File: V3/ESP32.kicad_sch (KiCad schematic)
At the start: 20 parts, among them J6 Conn_01x02_Female, Q6 MMBT2222, SW2 RST, SW3 BOOT, U9 ESP32-WROOM-32

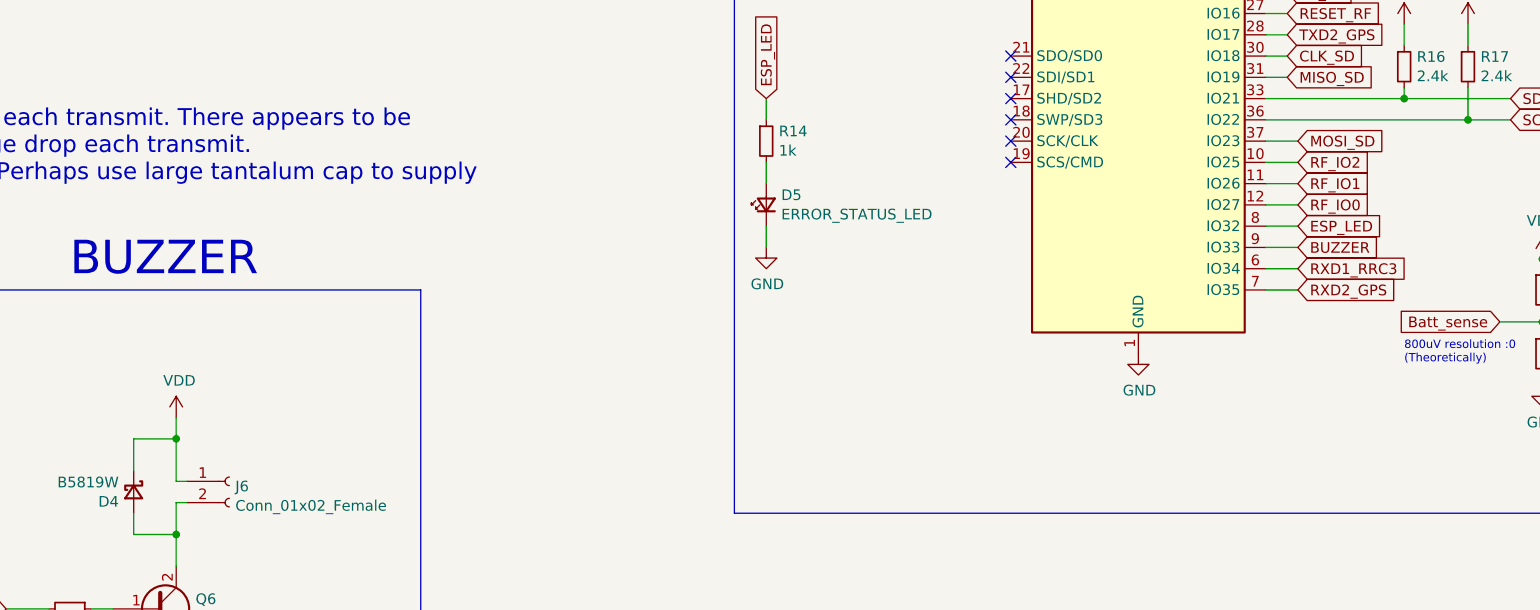
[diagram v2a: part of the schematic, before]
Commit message: Added mpu6050 back
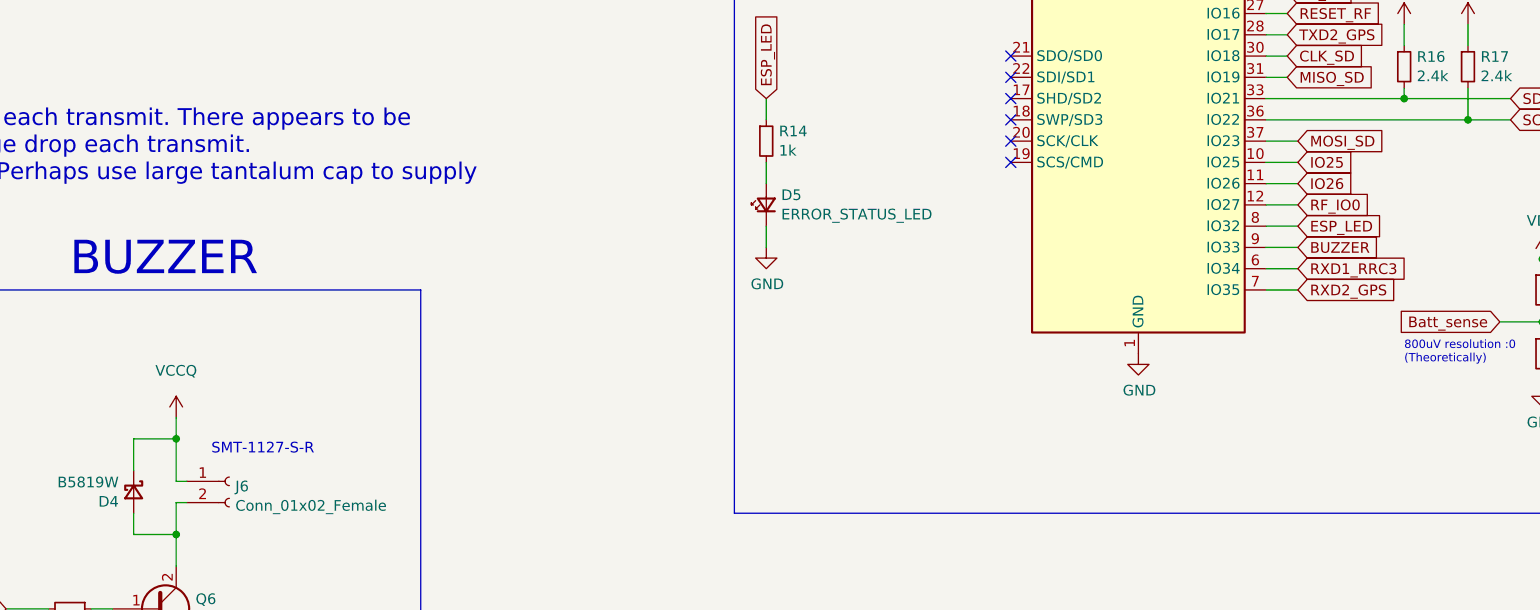
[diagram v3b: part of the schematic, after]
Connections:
- net VDD: no longer D4.1 (K), J6.1 (Pin_1)
- net RF_IO1 renamed IO26
- net RF_IO2 renamed IO25
- new net VCCQ: D4.1 (K), J6.1 (Pin_1)
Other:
- note added: "SMT-1127-S-R"
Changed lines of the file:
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@@
     (stroke (width 0) (type default) (color 0 0 0 0))
+  )
+  (text "SMT-1127-S-R" (at 83.566 138.557 0)
+    (effects (font (size 1.27 1.27)) (justify left bottom))
   )
   (text "Power LED flickers each transmit. There appears to be \na significant voltage drop each transmit.\nVerify with scope. Perhaps use large tantalum cap to supply \ntransmit current. "
@@
     )
   )
-  (global_label "RF_IO2" (shape input) (at 213.36 103.505 0) (fields_autoplaced)
-    (effects (font (size 1.27 1.27)) (justify left))
-    (property "Intersheet References" "${INTERSHEET_REFS}" (id 0) (at 124.46 -6.985 0)
-      (effects (font (size 1.27 1.27)) hide)
+  (global_label "IO25" (shape input) (at 213.36 103.505 0) (fields_autoplaced)
+    (effects (font (size 1.27 1.27)) (justify left))
+    (property "Intersheet References" "${INTERSHEET_REFS}" (id 0) (at 220.0385 103.4256 0)
+      (effects (font (size 1.27 1.27)) (justify left) hide)
     )
   )
@@
     )
   )
-  (global_label "RF_IO1" (shape input) (at 213.36 106.045 0) (fields_autoplaced)
-    (effects (font (size 1.27 1.27)) (justify left))
-    (property "Intersheet References" "${INTERSHEET_REFS}" (id 0) (at 124.46 -6.985 0)
-      (effects (font (size 1.27 1.27)) hide)
+  (global_label "IO26" (shape input) (at 213.36 106.045 0) (fields_autoplaced)
+    (effects (font (size 1.27 1.27)) (justify left))
+    (property "Intersheet References" "${INTERSHEET_REFS}" (id 0) (at 220.0385 105.9656 0)
+      (effects (font (size 1.27 1.27)) (justify left) hide)
     )
   )
@@
     (pin "9")
   )
+  (symbol (lib_id "power:VCCQ") (at 79.375 133.985 0) (unit 1)
+    (in_bom yes) (on_board yes) (fields_autoplaced)
+    (property "Reference" "#PWR?" (id 0) (at 79.375 137.795 0)
+      (effects (font (size 1.27 1.27)) hide)
+    )
+    (property "Value" "VCCQ" (id 1) (at 79.375 128.397 0))
+    (property "Footprint" "" (id 2) (at 79.375 133.985 0)
+      (effects (font (size 1.27 1.27)) hide)
+    )
+    (property "Datasheet" "" (id 3) (at 79.375 133.985 0)
+      (effects (font (size 1.27 1.27)) hide)
+    )
+    (pin "1")
+  )
   (symbol (lib_id "Connector:Conn_01x02_Female") (at 85.725 141.605 0) (unit 1)
     (in_bom yes) (on_board yes)
@@
       (effects (font (size 1.27 1.27)) hide)
     )
-    (pin "1")
-  )
-  (symbol (lib_id "power:VDD") (at 79.375 133.985 0) (unit 1)
-    (in_bom yes) (on_board yes)
-    (property "Reference" "#PWR0144" (id 0) (at 79.375 137.795 0)
-      (effects (font (size 1.27 1.27)) hide)
-    )
-    (property "Value" "VDD" (id 1) (at 79.756 129.5908 0))
-    (property "Footprint" "" (id 2) (at 79.375 133.985 0)
-      (effects (font (size 1.27 1.27)) hide)
-    )
-    (property "Datasheet" "" (id 3) (at 79.375 133.985 0)
-      (effects (font (size 1.27 1.27)) hide)
-    )

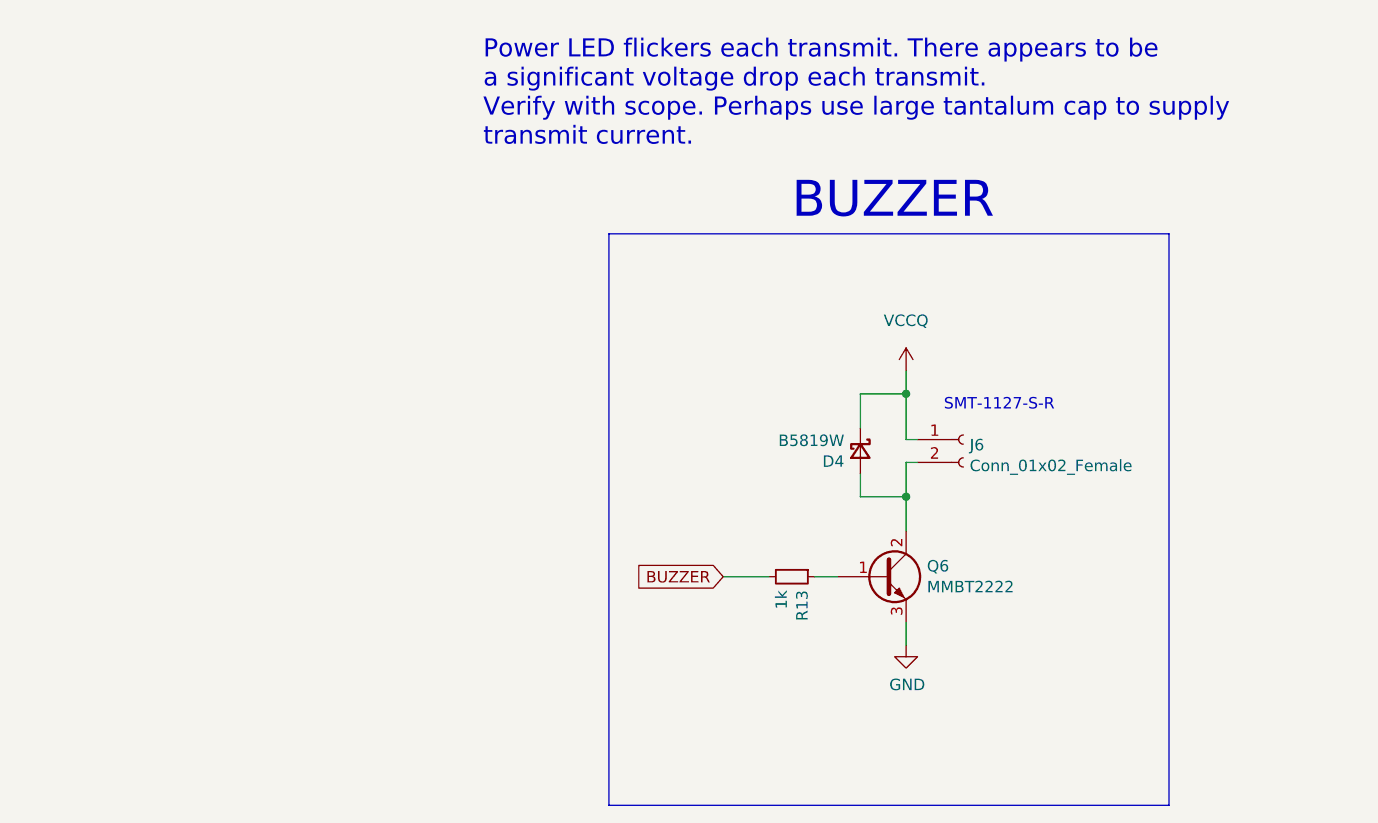
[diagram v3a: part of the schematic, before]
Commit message: buzzer added
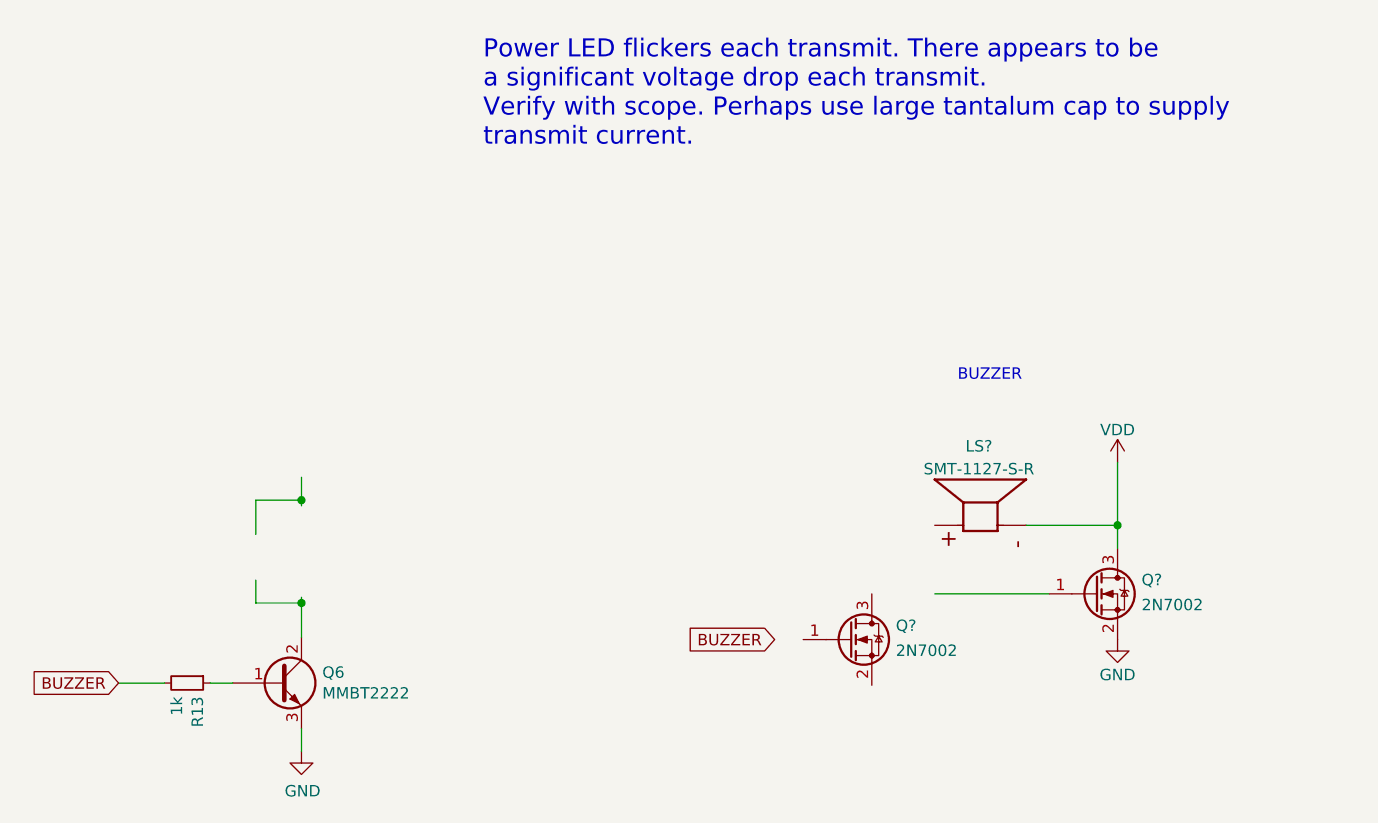
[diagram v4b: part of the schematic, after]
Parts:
- removed D4: B5819W, Diode_SMD:D_SOD-123, symbol Device:D_Schottky_Small
- removed J6: Conn_01x02_Female, Connector_PinSocket_2.54mm:PinSocket_1x02_P2.54mm_Vertical, symbol Connector:Conn_01x02_Female
- added LS?: SMT-1127-S-R, XDCR_SMT-1127-S-R, symbol SMT-1127-S-R:SMT-1127-S-R
- added Q? (x2): 2N7002, Package_TO_SOT_SMD:SOT-23, symbol Transistor_FET:2N7002
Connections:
- net GND: now also Q?.2 (S)
- net VDD: now also LS?.N, Q?.3 (D)
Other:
- note removed: "SMT-1127-S-R"
- moved on the sheet: Q6, R13

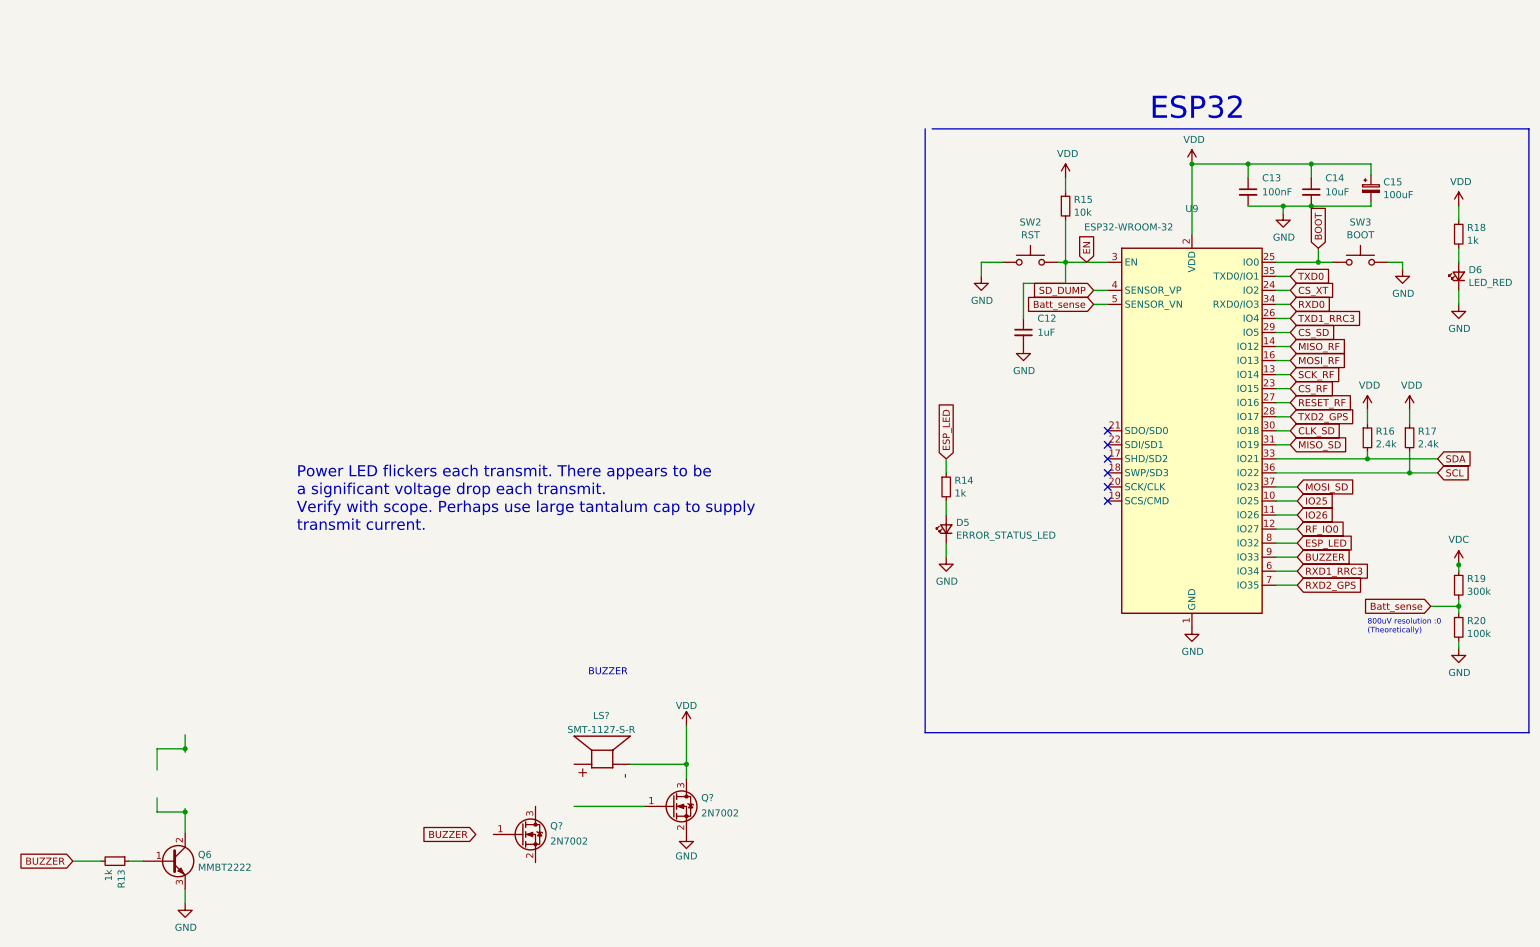
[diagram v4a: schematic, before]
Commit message: almost finished component placement
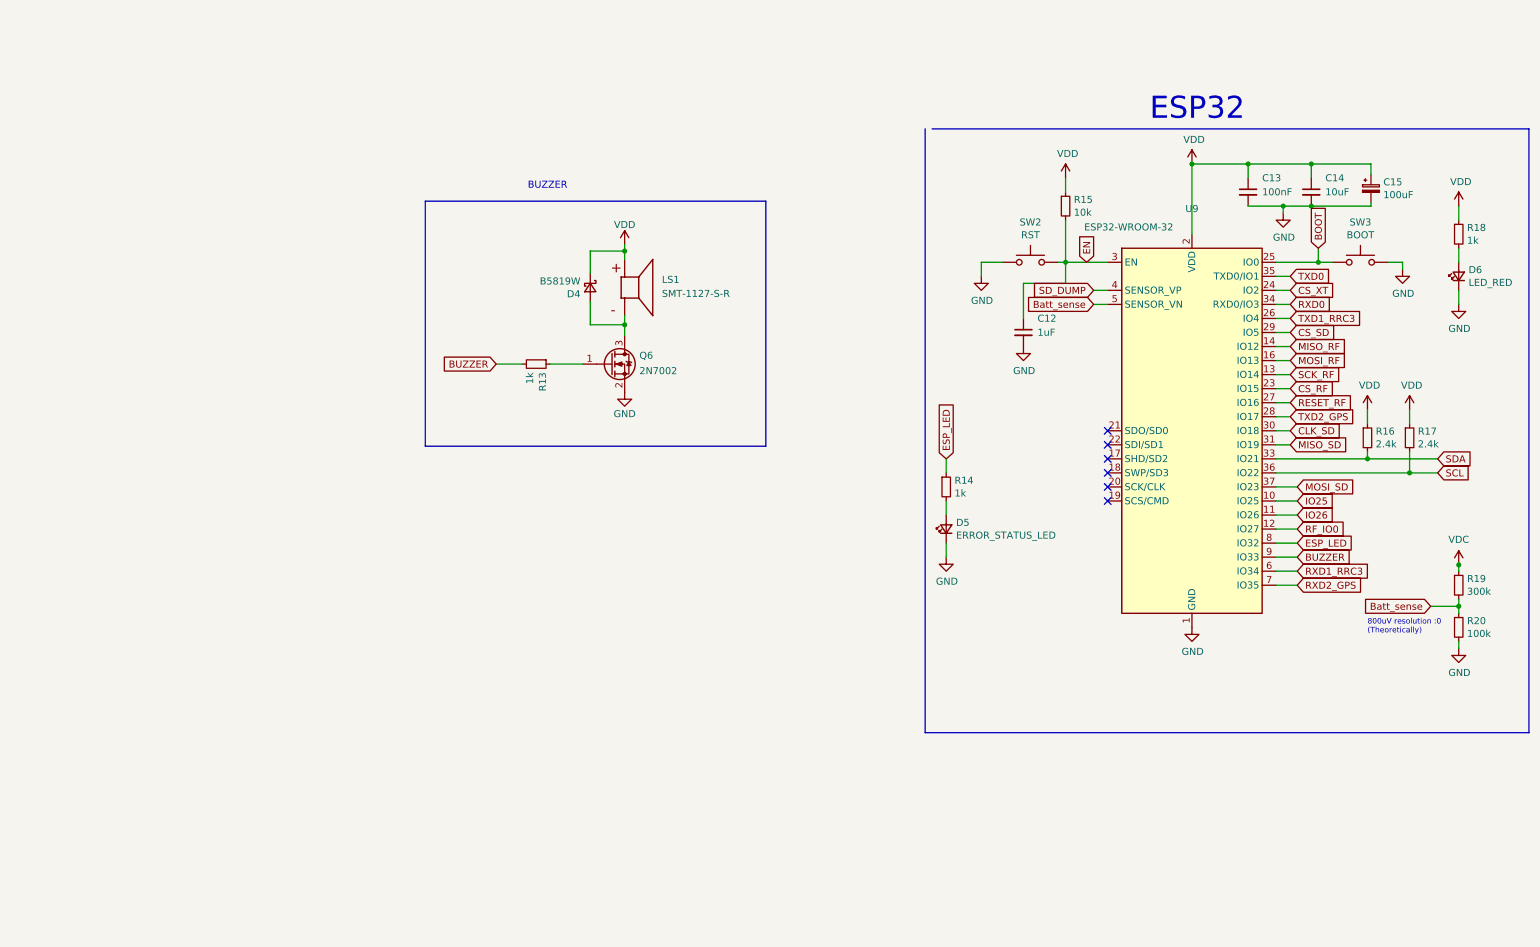
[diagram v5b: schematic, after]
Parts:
- removed Q6: MMBT2222, Package_TO_SOT_SMD:SOT-23, symbol Device:Q_NPN_BCE
- removed Q?: 2N7002, Package_TO_SOT_SMD:SOT-23, symbol Transistor_FET:2N7002
- added D4: B5819W, Diode_SMD:D_SOD-123, symbol Device:D_Schottky_Small
- gave numbers to parts that had none: 2
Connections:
- net VDD: now also LS1.P, D4.1 (K); no longer LS1.N, Q6.3 (D)
- net at Q6.1 (G): now also R13.1
- new net: D4.2 (A), LS1.N, Q6.3 (D)
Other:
- note removed: "Power LED flickers each transmit. There appears to be a significant voltage drop each transmit. Verify with scope. Perhaps use large tantalum cap to supply transmit current."
- moved on the sheet: LS1, Q6

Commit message: New parts placed and routed
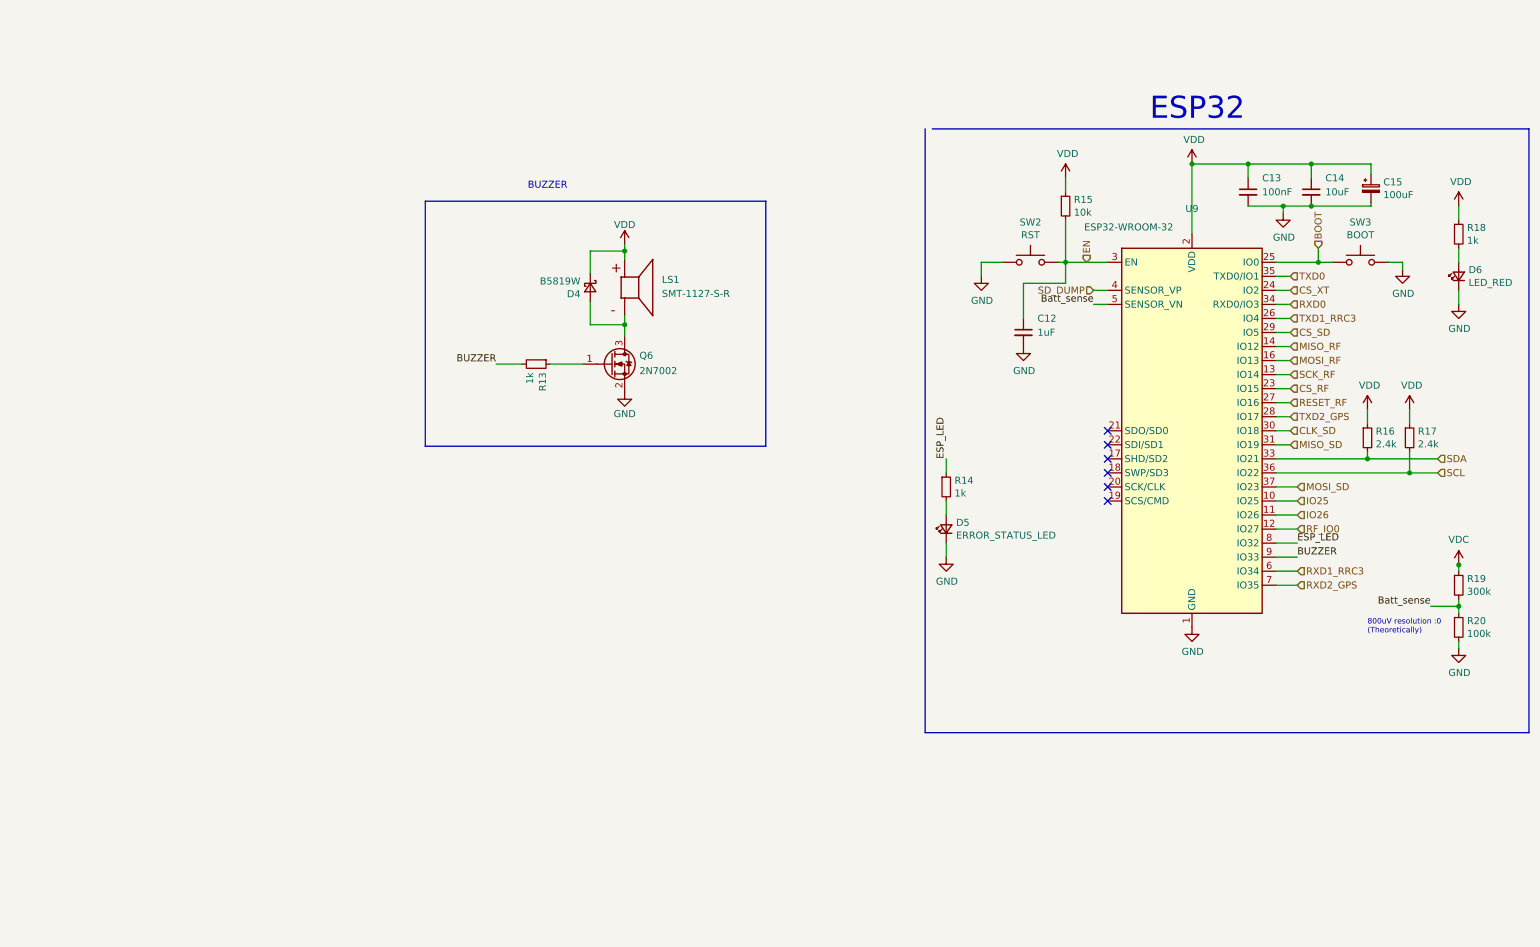
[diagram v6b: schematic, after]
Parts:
- LS1: footprint XDCR_SMT-1127-S-R -> Local_footprints:XDCR_SMT-1127-S-R
